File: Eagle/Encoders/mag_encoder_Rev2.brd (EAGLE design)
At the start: 9.9 x 26.8 mm, 7 parts, among them IC1 A1203LH

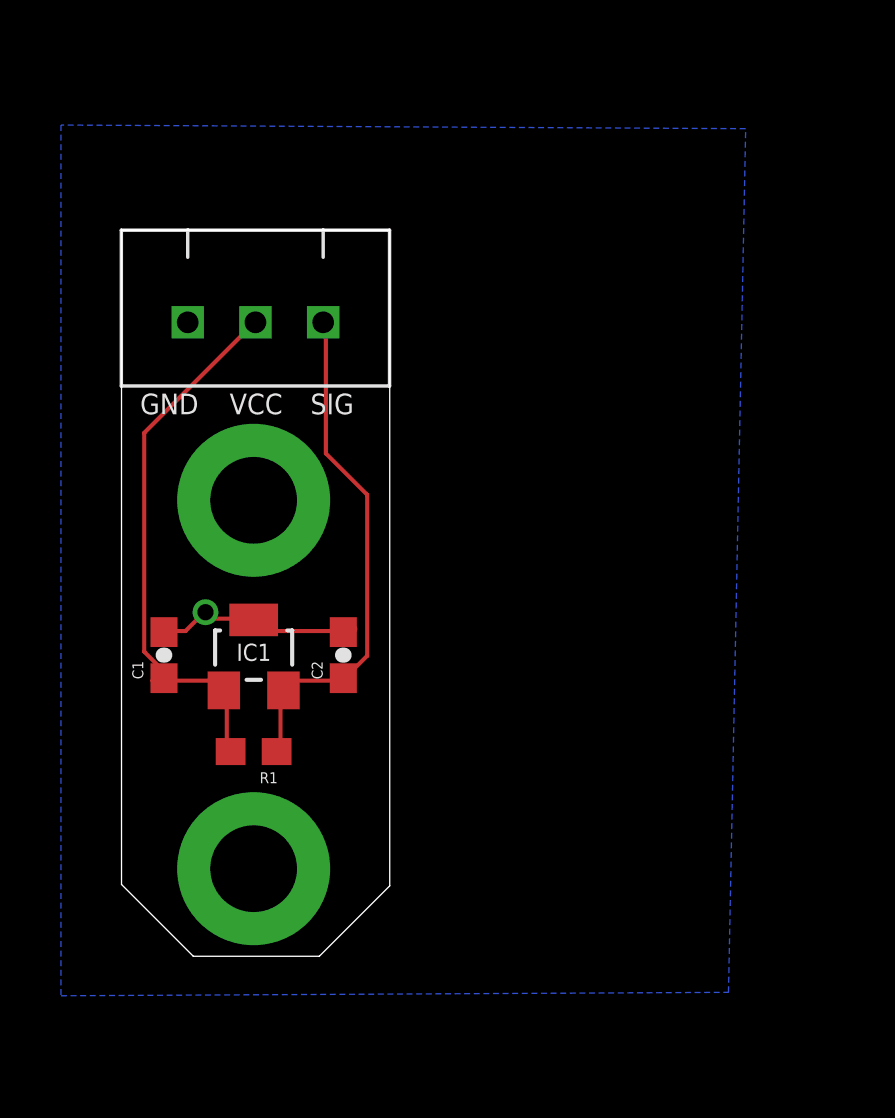
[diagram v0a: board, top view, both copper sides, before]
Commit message: Modified encoder boards and added modified revision.
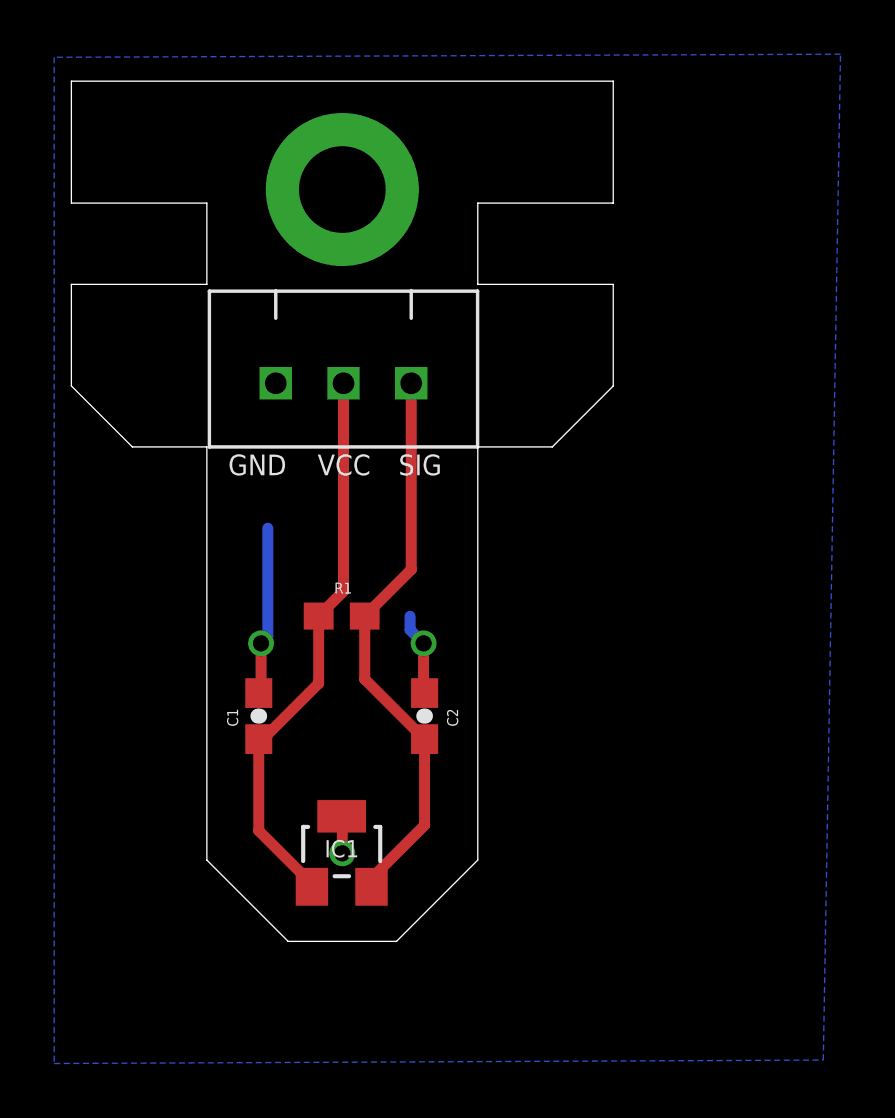
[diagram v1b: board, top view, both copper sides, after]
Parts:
- removed U$2: MOUNTING_SCREW-3MM, Clayton:MOUNTING_SCREW-3MM
- moved U$3 11.9 mm to (9.75, 29.2)
- moved IC1 7.95 mm to (9.73, 4.82)
- moved R1 5.96 mm to (9.73, 13.5)
- moved C1 4.16 mm to (6.67, 9.81)
- moved U$1 3.95 mm to (14.7, 25.5)
- moved C2 3.75 mm to (12.8, 9.81)
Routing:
- net GND: track 8.11 -> 10.9 mm, vias 1 -> 3
- net SIG: track 19.0 -> 20.8 mm
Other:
- board size 9.9 x 26.8 mm -> 20 x 31.8 mm
- board text added: "Magnetic Encoder Rev2"
- board text removed: "Magnetic Encoder Rev1"

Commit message: Modified encoder board and encoder Arduino code.
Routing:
- net GND: track 10.9 -> 7.51 mm
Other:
- outline, holes or cut-outs redrawn
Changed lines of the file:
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@@
 <setting verticaltext="up"/>
 </settings>
-<grid distance="0.25" unitdist="mm" unit="inch" style="lines" multiple="1" display="yes" altdistance="0.25" altunitdist="mm" altunit="mm"/>
+<grid distance="0.00984251969" unitdist="inch" unit="inch" style="lines" multiple="1" display="yes" altdistance="0.25" altunitdist="mm" altunit="mm"/>
 <layers>
 <layer number="1" name="Top" color="4" fill="1" visible="yes" active="yes"/>
@@
 <board>
 <plain>
-<text x="9.283" y="6.675" size="1.27" layer="26" rot="MR90">Magnetic Encoder Rev2</text>
+<text x="5.533" y="2.175" size="1.016" layer="26" rot="MR90">Magnetic Encoder Rev2</text>
 <text x="5.536" y="18.705" size="0.762" layer="25">GND</text>
 <text x="11.8225" y="18.705" size="0.762" layer="25">SIG</text>
 <text x="8.838" y="18.705" size="0.762" layer="25">VCC</text>
-<wire x1="4.75" y1="4.5" x2="4.75" y2="19.75" width="0" layer="20"/>
-<wire x1="19.75" y1="33.25" x2="19.75" y2="28.75" width="0" layer="20"/>
-<wire x1="-0.25" y1="33.25" x2="-0.25" y2="28.75" width="0" layer="20"/>
-<wire x1="14.75" y1="19.75" x2="14.75" y2="4.5" width="0" layer="20"/>
-<wire x1="-0.25" y1="33.25" x2="19.75" y2="33.25" width="0" layer="20"/>
+<wire x1="4.75" y1="1.5" x2="4.75" y2="19.75" width="0" layer="20"/>
+<wire x1="19.75" y1="31" x2="19.75" y2="28.75" width="0" layer="20"/>
+<wire x1="-0.25" y1="31" x2="-0.25" y2="28.75" width="0" layer="20"/>
+<wire x1="14.75" y1="19.75" x2="14.75" y2="1.5" width="0" layer="20"/>
+<wire x1="2" y1="33.25" x2="17.5" y2="33.25" width="0" layer="20"/>
 <wire x1="19.75" y1="22" x2="19.75" y2="25.75" width="0" layer="20"/>
 <wire x1="-0.25" y1="22" x2="-0.25" y2="25.75" width="0" layer="20"/>
 <wire x1="14.75" y1="19.75" x2="17.5" y2="19.75" width="0" layer="20"/>
 <wire x1="4.75" y1="19.75" x2="2" y2="19.75" width="0" layer="20"/>
-<wire x1="14.75" y1="4.5" x2="11.75" y2="1.5" width="0" layer="20"/>
-<wire x1="11.75" y1="1.5" x2="7.75" y2="1.5" width="0" layer="20"/>
-<wire x1="7.75" y1="1.5" x2="4.75" y2="4.5" width="0" layer="20"/>
+<wire x1="14.75" y1="1.5" x2="4.75" y2="1.5" width="0" layer="20"/>
 <wire x1="17.5" y1="19.75" x2="19.75" y2="22" width="0" layer="20"/>
 <wire x1="2" y1="19.75" x2="-0.25" y2="22" width="0" layer="20"/>
@@
 <dimension x1="-0.25" y1="28.75" x2="-0.25" y2="33.25" x3="-6.75" y3="31" textsize="1.778" layer="49" dtype="vertical"/>
 <dimension x1="17.5" y1="19.75" x2="17.25" y2="4.75" x3="19.75" y3="12.25" textsize="1.778" layer="49" dtype="vertical"/>
+<wire x1="19.75" y1="31" x2="17.5" y2="33.25" width="0" layer="20"/>
+<wire x1="2" y1="33.25" x2="-0.25" y2="31" width="0" layer="20"/>
 </plain>
 <attributes>
@@
 <contactref element="C1" pad="2"/>
 <contactref element="U$1" pad="P$3"/>
-<wire x1="6.667" y1="10.665" x2="6.75" y2="10.748" width="0.4064" layer="1"/>
-<wire x1="6.75" y1="10.748" x2="6.75" y2="12.5" width="0.4064" layer="1"/>
-<via x="6.75" y="12.5" extent="1-16" drill="0.6"/>
-<wire x1="6.75" y1="12.5" x2="7" y2="12.75" width="0.4064" layer="16"/>
-<wire x1="7" y1="12.75" x2="7" y2="16.75" width="0.4064" layer="16"/>
 <wire x1="9.727" y1="6.115" x2="9.75" y2="6.092" width="0.4064" layer="1"/>
 <wire x1="9.75" y1="6.092" x2="9.75" y2="4.75" width="0.4064" layer="1"/>
 <via x="9.75" y="4.75" extent="1-16" drill="0.6"/>
 <wire x1="9.75" y1="4.75" x2="9.75" y2="4.5" width="0.4064" layer="16"/>
-<wire x1="12.787" y1="10.665" x2="12.75" y2="10.702" width="0.4064" layer="1"/>
-<wire x1="12.75" y1="10.702" x2="12.75" y2="12.5" width="0.4064" layer="1"/>
-<via x="12.75" y="12.5" extent="1-16" drill="0.6"/>
-<wire x1="12.75" y1="12.5" x2="12.25" y2="13" width="0.4064" layer="16"/>
-<wire x1="12.25" y1="13" x2="12.25" y2="13.5" width="0.4064" layer="16"/>
+<wire x1="6.667" y1="10.665" x2="6.667" y2="12.167" width="0.4064" layer="1"/>
+<wire x1="6.667" y1="12.167" x2="7.25" y2="12.75" width="0.4064" layer="1"/>
+<via x="7.25" y="12.75" extent="1-16" drill="0.6"/>
+<wire x1="7.25" y1="12.75" x2="7.25" y2="13.25" width="0.4064" layer="16"/>
+<wire x1="12.787" y1="10.665" x2="12.787" y2="12.213" width="0.4064" layer="1"/>
+<wire x1="12.787" y1="12.213" x2="12.25" y2="12.75" width="0.4064" layer="1"/>
+<via x="12.25" y="12.75" extent="1-16" drill="0.6"/>
+<wire x1="12.25" y1="12.75" x2="12.25" y2="13.5" width="0.4064" layer="16"/>
 </signal>
 <signal name="VCC">
